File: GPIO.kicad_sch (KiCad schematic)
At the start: 20 parts, among them J7 Conn_01x08, Q8 , Q9 , U10 MAX22193

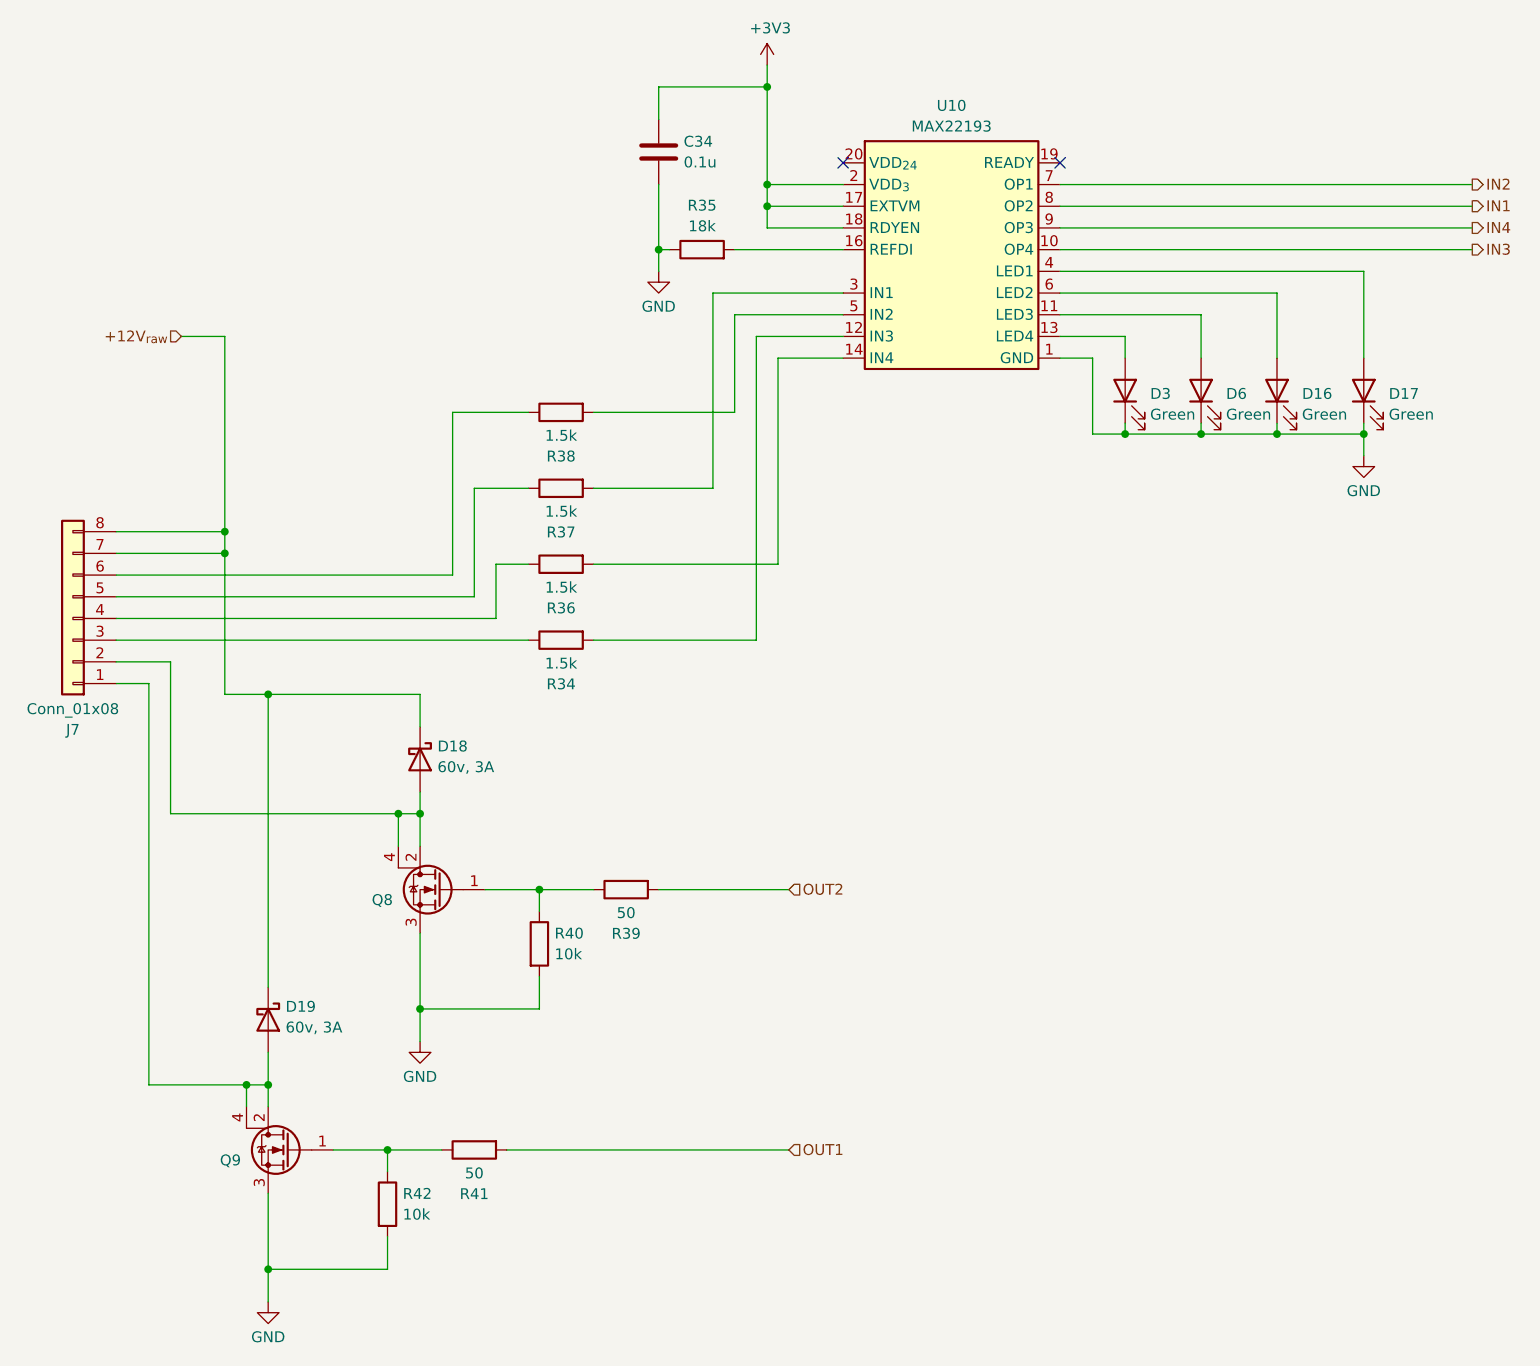
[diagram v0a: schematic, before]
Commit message: revised schematic after initial layout  - all connectors are vertical  - increased current handling of outputs  - replaced mechanical relay with ssr  - jumper to disable gps antenna power
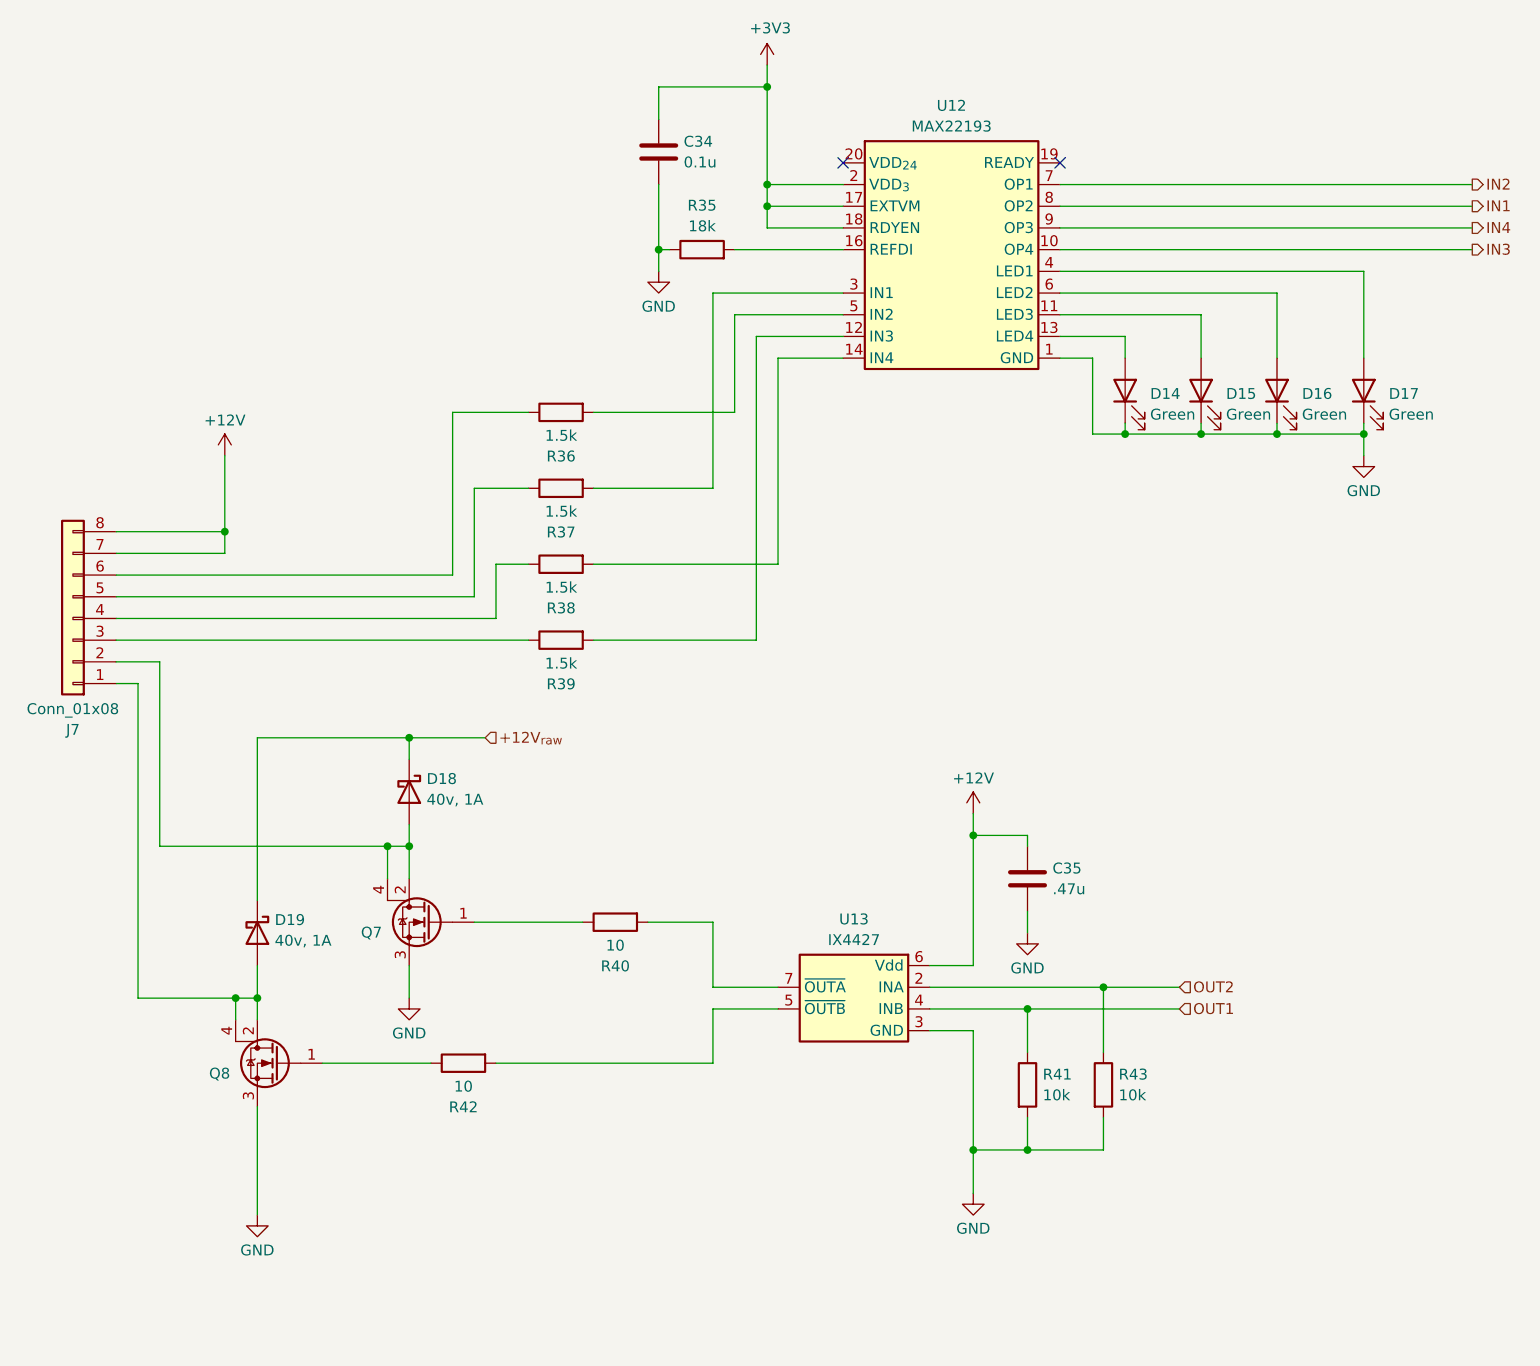
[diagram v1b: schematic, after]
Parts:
- removed Q9: (no value), Package_TO_SOT_SMD:SOT-223, symbol Device:Q_NMOS_GDSD
- added C35: .47u, Capacitor_SMD:C_0805_2012Metric, symbol Device:C
- added Q7: (no value), Package_SON:Infineon_PG-TDSON-8_6.15x5.15mm, symbol Device:Q_NMOS_GDSD
- added U13: IX4427, Package_DFN_QFN:DFN-8-1EP_3x3mm_P0.65mm_EP1.7x2.05mm, symbol Custom:IX4427
- C34: footprint Capacitor_SMD:C_0603_1608Metric_Pad1.08x0.95mm_HandSolder -> Capacitor_SMD:C_0603_1608Metric
- D14: renamed from D3; footprint LED_SMD:LED_0603_1608Metric_Pad1.05x0.95mm_HandSolder -> LED_SMD:LED_0603_1608Metric
- D15: renamed from D6; footprint LED_SMD:LED_0603_1608Metric_Pad1.05x0.95mm_HandSolder -> LED_SMD:LED_0603_1608Metric
- D16, D17: footprint LED_SMD:LED_0603_1608Metric_Pad1.05x0.95mm_HandSolder -> LED_SMD:LED_0603_1608Metric
- D18, D19: value 60v, 3A -> 40v, 1A; footprint Diode_SMD:D_PowerDI-123 -> Diode_SMD:D_SOD-323F; Mfg Part Number SBR3U60P1Q -> PMEG4010EJ,115
- Q8: footprint Package_TO_SOT_SMD:SOT-223 -> Package_SON:Infineon_PG-TDSON-8_6.15x5.15mm; Mfg Part Number BUK9832-55A/CUX -> SIRA54ADP-T1-RE3
- R35, R37: footprint Resistor_SMD:R_0603_1608Metric_Pad0.98x0.95mm_HandSolder -> Resistor_SMD:R_0603_1608Metric
- R36: renamed from R38; footprint Resistor_SMD:R_0603_1608Metric_Pad0.98x0.95mm_HandSolder -> Resistor_SMD:R_0603_1608Metric
- R38: renamed from R36; footprint Resistor_SMD:R_0603_1608Metric_Pad0.98x0.95mm_HandSolder -> Resistor_SMD:R_0603_1608Metric
- R39: renamed from R34; footprint Resistor_SMD:R_0603_1608Metric_Pad0.98x0.95mm_HandSolder -> Resistor_SMD:R_0603_1608Metric
- R40: renamed from R39; value 50 -> 10; footprint Resistor_SMD:R_0603_1608Metric_Pad0.98x0.95mm_HandSolder -> Resistor_SMD:R_0603_1608Metric
- R41: renamed from R40; footprint Resistor_SMD:R_0603_1608Metric_Pad0.98x0.95mm_HandSolder -> Resistor_SMD:R_0603_1608Metric
- R42: renamed from R41; value 50 -> 10; footprint Resistor_SMD:R_0603_1608Metric_Pad0.98x0.95mm_HandSolder -> Resistor_SMD:R_0603_1608Metric
- R43: renamed from R42; footprint Resistor_SMD:R_0603_1608Metric_Pad0.98x0.95mm_HandSolder -> Resistor_SMD:R_0603_1608Metric
- renumbered U10 to U12
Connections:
- net +12V_{raw}: no longer J7.7 (Pin_7), J7.8 (Pin_8)
- net GND: now also C35.2, Q7.3 (S), U13.3 (GND)
- net OUT1: now also R41.1, U13.4 (INB); no longer R42.2
- net OUT2: now also R43.1, U13.2 (INA); no longer R40.2
- net at D19.2 (A), J7.1 (Pin_1): now also Q8.2 (D), Q8.4 (D)
- net at D18.2 (A), J7.2 (Pin_2): now also Q7.2 (D), Q7.4 (D); no longer Q8.2 (D), Q8.4 (D)
- net at R42.1: now also Q8.1 (G); no longer R43.1
- new net: Q7.1 (G), R40.1
- new net: R40.2, U13.7 (~{OUTA})
- new net: R42.2, U13.5 (~{OUTB})
- new net +12V: C35.1, J7.7 (Pin_7), J7.8 (Pin_8), U13.6 (Vdd)
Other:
- moved on the sheet: D18, R40, R41, R42, R43

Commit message: second pass at layout complete
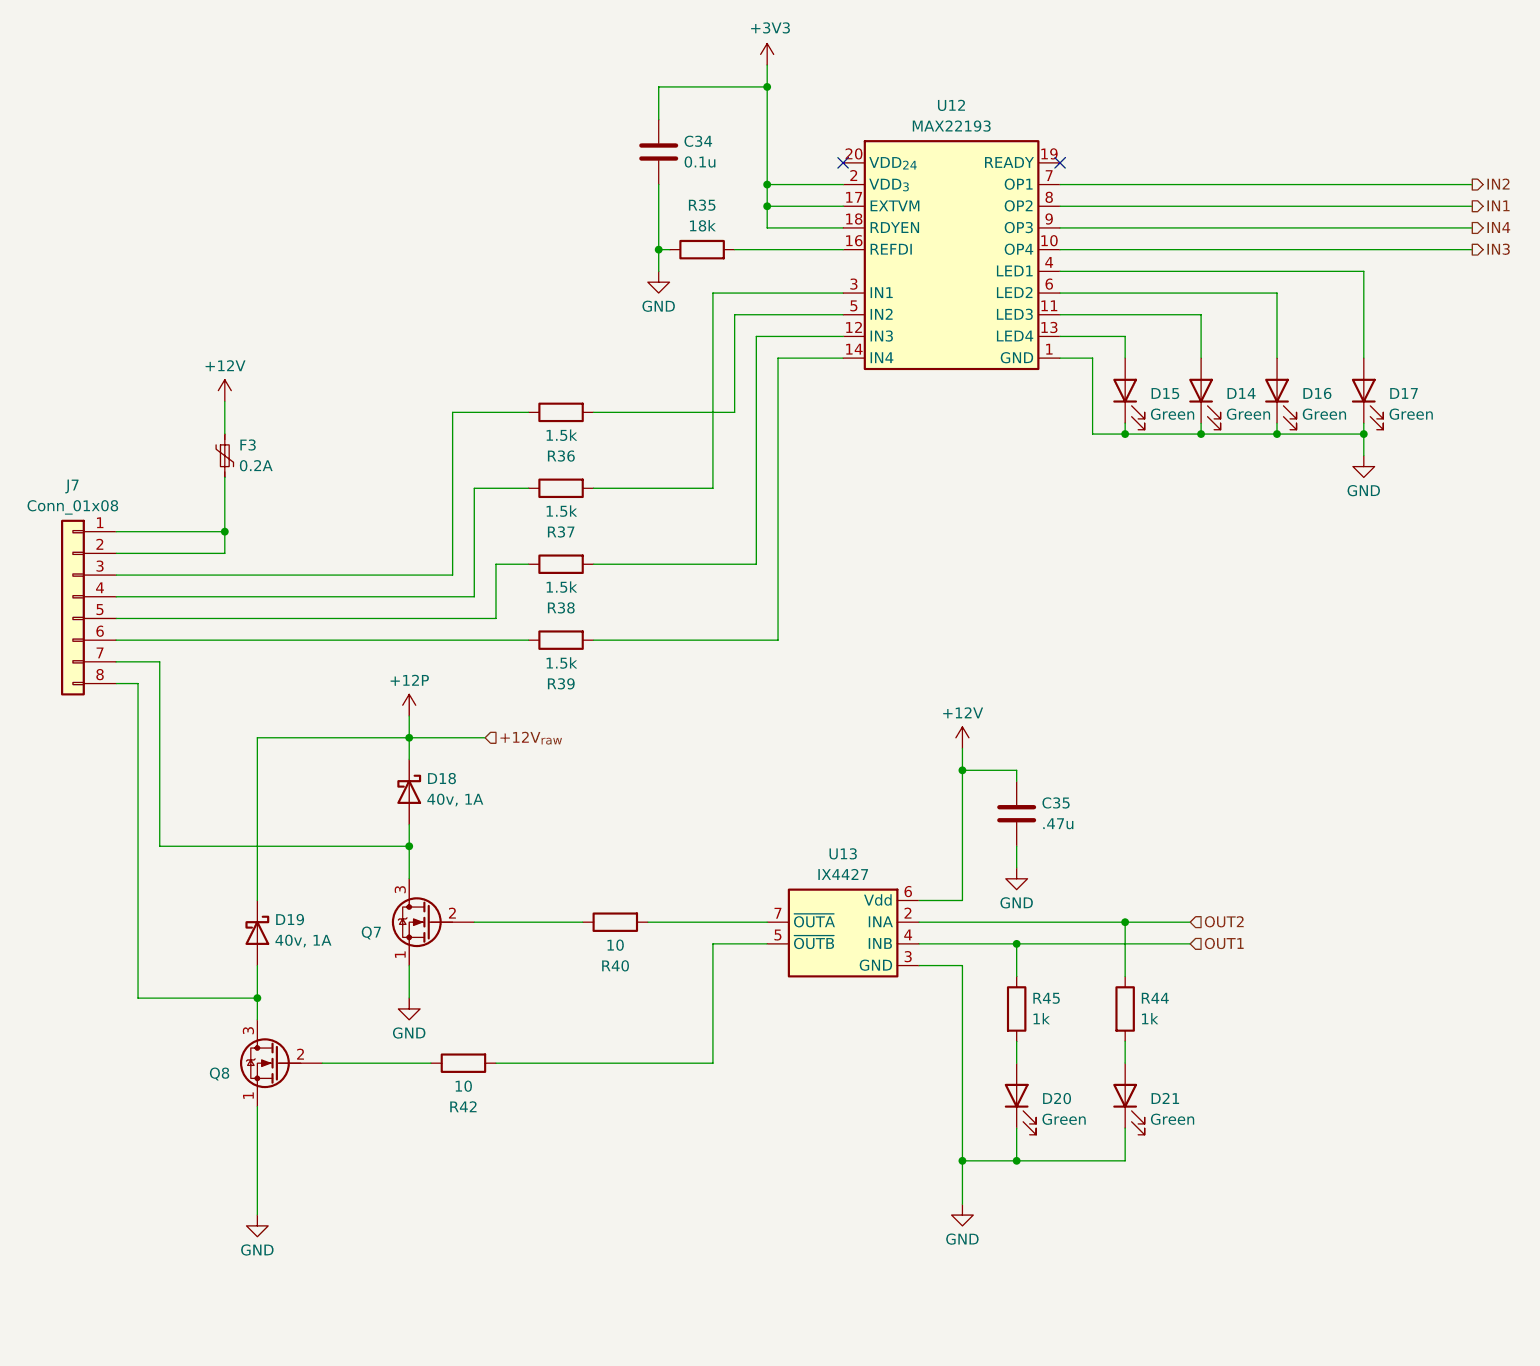
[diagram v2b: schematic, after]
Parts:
- removed R41, R43: 10k, Resistor_SMD:R_0603_1608Metric, symbol Device:R
- added D20, D21: Green, LED_SMD:LED_0603_1608Metric, symbol Device:LED
- added F3: 0.2A, Fuse:Fuse_1812_4532Metric, symbol Device:Polyfuse_Small
- added R44, R45: 1k, Resistor_SMD:R_0603_1608Metric, symbol Device:R
- J7: footprint Connector_JST:JST_PH_B8B-PH-K_1x08_P2.00mm_Vertical -> Connector_Molex:Molex_Nano-Fit_105309-xx08_1x08_P2.50mm_Vertical
- Q7, Q8: symbol Device:Q_NMOS_GDSD -> Device:Q_NMOS_SGD
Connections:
- net +12V: now also F3.1; no longer J7.7 (Pin_7), J7.8 (Pin_8)
- net GND: now also Q7.1 (S), Q8.1 (S), D20.1 (K), D21.1 (K); no longer Q7.3 (S), Q8.3 (S)
- net OUT1: now also R45.1
- net OUT2: now also R44.1
- net at J7.3 (Pin_3): now also R36.1; no longer R39.1
- net at J7.4 (Pin_4): now also R37.1; no longer R38.1
- net at J7.5 (Pin_5): now also R38.1; no longer R37.1
- net at J7.6 (Pin_6): now also R39.1; no longer R36.1
- net at U12.11 (LED3): now also D14.2 (A); no longer D15.2 (A)
- net at U12.12 (IN3): now also R38.2; no longer R39.2
- net at U12.13 (LED4): now also D15.2 (A); no longer D14.2 (A)
- net at U12.14 (IN4): now also R39.2; no longer R38.2
- net at R40.1: now also Q7.2 (G); no longer Q7.1 (G)
- net at R42.1: now also Q8.2 (G); no longer Q8.1 (G)
- net +12V_{raw} renamed +12P
- new net: F3.2, J7.1 (Pin_1), J7.2 (Pin_2)
- new net: D18.2 (A), J7.7 (Pin_7), Q7.3 (D)
- new net: D19.2 (A), J7.8 (Pin_8), Q8.3 (D)
- new net: D21.2 (A), R44.2
- new net: D20.2 (A), R45.2
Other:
- moved on the sheet: C35, D14, D15, J7, U13

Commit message: filled in mfg part number for ordering
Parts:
- J7: Mfg Part Number (none) -> 105309-1208
- U12: Mfg Part Number (none) -> MAX22193ATP+
- U13: Mfg Part Number (none) -> IX4427MTR
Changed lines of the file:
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@@
+			)
+		)
+		(property "Mfg Part Number" "105309-1208"
+			(at 55.88 86.36 0)
+			(effects
+				(font
+					(size 1.27 1.27)
+				)
+				(hide yes)
 			)
 		)
@@
 			)
 		)
+		(property "Mfg Part Number" "MAX22193ATP+"
+			(at 158.75 46.99 0)
+			(effects
+				(font
+					(size 1.27 1.27)
+				)
+				(hide yes)
+			)
+		)
 		(pin "7"
 		)
@@
 			(effects
 				(font
+					(size 1.27 1.27)
+				)
+				(hide yes)
+			)
+		)
+		(property "Mfg Part Number" "IX4427MTR"
+			(at 146.05 125.73 0)
+			(effects
+				(font

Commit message: bug fixes from testing
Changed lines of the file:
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@@
-	(wire
-		(pts
-			(xy 95.25 102.87) (xy 104.14 102.87)
-		)
-		(stroke
-			(width 0)
-			(type default)
-		)
-	)
 	(wire
 		(pts
@@
 		(fields_autoplaced yes)
 		(effects
-			(font
-				(size 1.27 1.27)
-			)
-			(justify left)
-		)
-	)
-	(hierarchical_label "+12V_{raw}"
-		(shape input)
-		(at 104.14 102.87 0)
-		(fields_autoplaced yes)
-		(effects

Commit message: fixes from testing, updated for pi5
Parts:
- R35: value 18k -> 5.1k
- R36, R37, R38, R39: value 1.5k -> 430
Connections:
- net at D18.2 (A), Q7.3 (D): now also J7.8 (Pin_8); no longer J7.7 (Pin_7)
- net at D19.2 (A), Q8.3 (D): now also J7.7 (Pin_7); no longer J7.8 (Pin_8)
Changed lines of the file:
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@@
 	(wire
 		(pts
-			(xy 171.45 43.18) (xy 219.71 43.18)
+			(xy 66.04 96.52) (xy 66.04 115.57)
 		)
 		(stroke
@@
 	(wire
 		(pts
-			(xy 160.02 152.4) (xy 160.02 129.54)
+			(xy 171.45 43.18) (xy 219.71 43.18)
 		)
 		(stroke
@@
 	(wire
 		(pts
-			(xy 160.02 104.14) (xy 160.02 106.68)
+			(xy 160.02 152.4) (xy 160.02 129.54)
 		)
 		(stroke
@@
 	(wire
 		(pts
-			(xy 73.66 72.39) (xy 73.66 78.74)
+			(xy 160.02 104.14) (xy 160.02 106.68)
 		)
 		(stroke
@@
 	(wire
 		(pts
-			(xy 166.37 127) (xy 166.37 130.81)
+			(xy 73.66 72.39) (xy 73.66 78.74)
 		)
 		(stroke
@@
 	(wire
 		(pts
-			(xy 137.16 26.67) (xy 137.16 38.1)
+			(xy 166.37 127) (xy 166.37 130.81)
 		)
 		(stroke
@@
 	(wire
 		(pts
-			(xy 135.89 55.88) (xy 135.89 82.55)
+			(xy 137.16 26.67) (xy 137.16 38.1)
 		)
 		(stroke
@@
 	(wire
 		(pts
-			(xy 187.96 53.34) (xy 187.96 58.42)
+			(xy 135.89 55.88) (xy 135.89 82.55)
 		)
 		(stroke
@@
 	(wire
 		(pts
-			(xy 60.96 93.98) (xy 66.04 93.98)
+			(xy 187.96 53.34) (xy 187.96 58.42)
 		)
 		(stroke
@@
 	(wire
 		(pts
+			(xy 63.5 93.98) (xy 63.5 133.35)
+		)
+		(stroke
+			(width 0)
+			(type default)
+		)
+	)
+	(wire
+		(pts
 			(xy 166.37 127) (xy 186.69 127)
 		)
@@
 	(wire
 		(pts
-			(xy 66.04 93.98) (xy 66.04 115.57)
-		)
-		(stroke
-			(width 0)
-			(type default)
-		)
-	)
-	(wire
-		(pts
 			(xy 175.26 58.42) (xy 171.45 58.42)
 		)
@@
 	(wire
 		(pts
-			(xy 175.26 67.31) (xy 175.26 58.42)
+			(xy 60.96 93.98) (xy 63.5 93.98)
 		)
 		(stroke
@@
 	(wire
 		(pts
-			(xy 137.16 127) (xy 130.81 127)
+			(xy 175.26 67.31) (xy 175.26 58.42)
 		)
 		(stroke
@@
 	(wire
 		(pts
-			(xy 137.16 40.64) (xy 137.16 38.1)
+			(xy 137.16 127) (xy 130.81 127)
 		)
 		(stroke
@@
 	(wire
 		(pts
-			(xy 63.5 96.52) (xy 60.96 96.52)
+			(xy 137.16 40.64) (xy 137.16 38.1)
 		)
 		(stroke
@@
 	(wire
 		(pts
-			(xy 63.5 133.35) (xy 63.5 96.52)
-		)
-		(stroke
-			(width 0)
-			(type default)
-		)
-	)
-	(wire
-		(pts
 			(xy 130.81 50.8) (xy 146.05 50.8)
 		)
@@
 	(wire
 		(pts
+			(xy 60.96 96.52) (xy 66.04 96.52)
+		)
+		(stroke
+			(width 0)
+			(type default)
+		)
+	)
+	(wire
+		(pts
 			(xy 77.47 133.35) (xy 77.47 135.89)
 		)
@@
 			)
 		)
-		(property "Value" "1.5k"
+		(property "Value" "430"
 			(at 113.03 76.3962 90)
 			(effects
@@
 			)
 		)
-		(property "Value" "18k"
+		(property "Value" "5.1k"
 			(at 129.54 42.9838 90)
 			(effects
@@
 			)
 		)
-		(property "Value" "1.5k"
+		(property "Value" "430"
 			(at 113.03 94.1762 90)
 			(effects
@@
 			)
 		)
-		(property "Value" "1.5k"
+		(property "Value" "430"
 			(at 113.03 67.5062 90)
 			(effects
@@
 			)
 		)
-		(property "Value" "1.5k"
+		(property "Value" "430"
 			(at 113.03 85.2862 90)
 			(effects
